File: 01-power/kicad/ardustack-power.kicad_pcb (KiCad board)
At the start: 2 copper layers, 68.6 x 53.3 mm, 14 parts, among them IC1 MC7805CTG, IC2 LP2950-33LPRE3, J1 CON-SOCJ-2155, P1 Power, P2 Analog, P3 Digital, P4 Digital, P5 CONN_01X01, P6 CONN_01X01, P7 CONN_01X01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

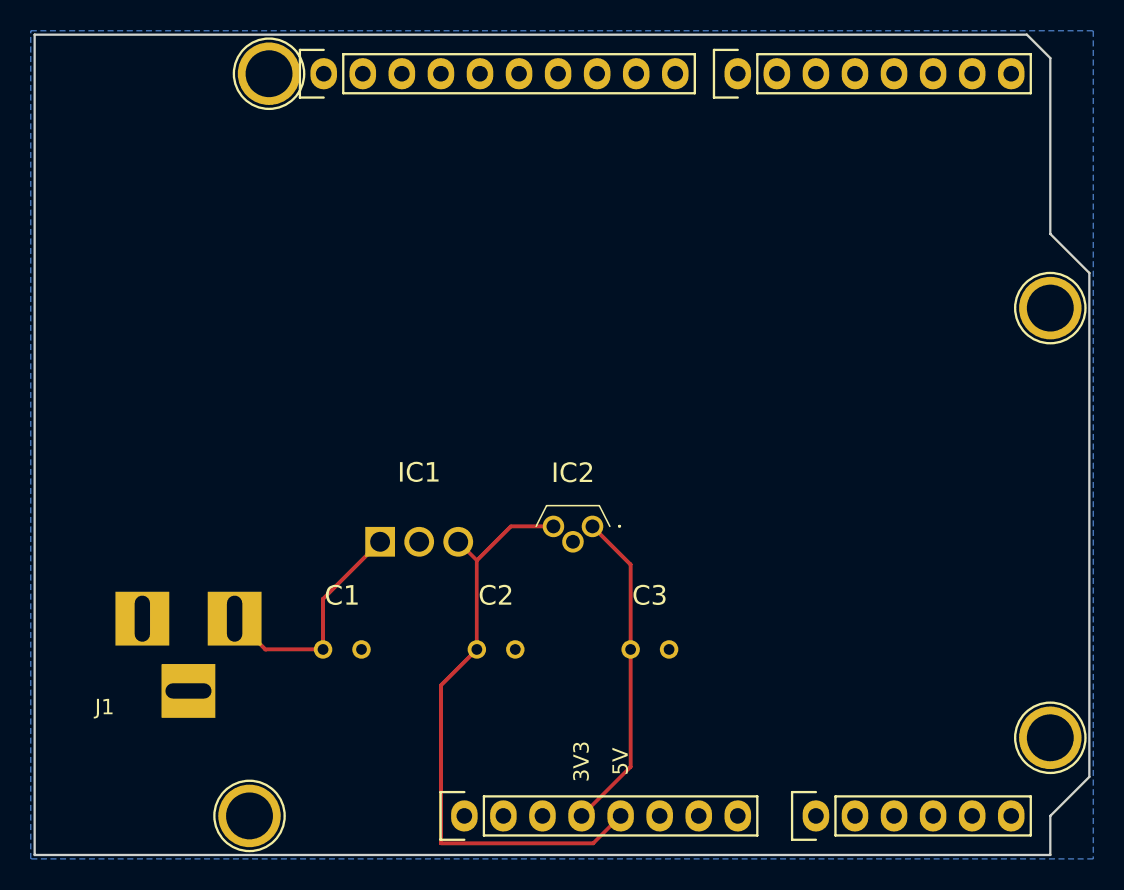
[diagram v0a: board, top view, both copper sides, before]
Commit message: Updates Ardustack power board PCB silkscreen
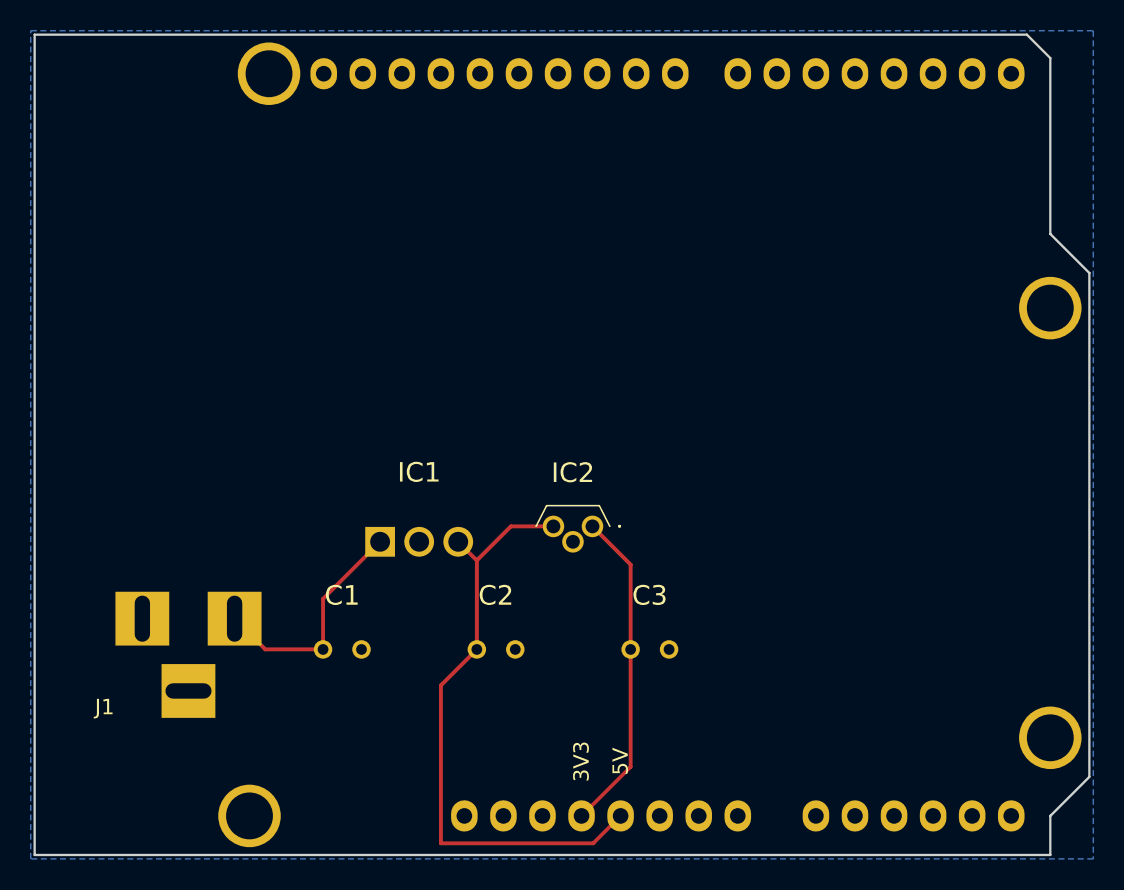
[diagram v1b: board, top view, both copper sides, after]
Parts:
- added G***: LOGO, ardustack-power:emblem, B.Cu at (160.0, 92.0)
- added G***: LOGO, ardustack-power:name_plate, B.Cu at (130.0, 90.0)

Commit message: Updates PCBs with name and version
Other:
- board text added: "ARDUSTACK POWER PCB v0.9.0"
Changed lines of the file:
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@@
   (gr_line (start 175.514 73.025) (end 110.998 73.025) (layer "Edge.Cuts") (width 0.15))
   (gr_line (start 177.038 85.979) (end 177.038 74.549) (layer "Edge.Cuts") (width 0.15))
+  (gr_text "ARDUSTACK POWER PCB v0.9.0" (at 133.1 78.9) (layer "B.SilkS")
+    (effects (font (size 1 1) (thickness 0.15)) (justify mirror))
+  )
   (gr_text "5V" (at 149.098 120.285 90) (layer "F.SilkS")
     (effects (font (size 1 1) (thickness 0.15)))

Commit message: Updates power, processor, and I/O boards to v1.0.0
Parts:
- moved C1 1.00 mm to (131.0, 112.0)
- moved C2 1.00 mm to (141.0, 112.0)
- moved C3 1.00 mm to (151.0, 112.0)
- moved IC1 1.00 mm to (136.0, 105.0)
- moved IC2 1.00 mm to (146.0, 104.0)
- moved J1 1.00 mm to (124.0, 112.0)
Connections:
- C1 pad 1: Net-(C1-Pad1) -> /Vin
- IC1 pad 1: Net-(C1-Pad1) -> /Vin
- J1 pad 1: Net-(C1-Pad1) -> /Vin
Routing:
- net /Vin: track 0.00 -> 50.7 mm
- net Net-(C1-Pad1): track 15.1 -> 0.00 mm
- net +3V3: track 21.2 -> 22.2 mm
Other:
- board text added: "(2)"
- board text added: "(3)"
- board text added: "(4)"
- board text added: "(5)"
- board text added: "(6)"
- board text added: "(7)"
- board text added: "(8)"
- board text added: "(9)"
- board text added: "(A0)"
- board text added: "(A1)"
- board text added: "(A2)"
- board text added: "(A3)"
- board text added: "(AREF)"
- board text added: "(IOREF)"
- board text added: "(MISO)"
- board text added: "(MOSI)"
- board text added: "(Reset)"
- board text added: "(Rx)"
- board text added: "(SCK)"
- board text added: "(SCL)"
- board text added: "(SDA)"
- board text added: "(SS)"
- board text added: "(Tx)"
- board text added: "+3V3"
- board text added: "+5V"
- board text added: "ARDUSTACK POWER PCB v1.0.0"
- board text added: "GND"
- board text added: "NC"
- board text added: "Vin"
- board text removed: "3V3"
- board text removed: "5V"
- board text removed: "ARDUSTACK POWER PCB v0.9.0"
